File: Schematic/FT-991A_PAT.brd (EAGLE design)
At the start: 44.6 x 59.8 mm, 50 parts, among them Q1 SN74AHC-OR, Q10 PE4259, Q2 PE4259, Q3 NCP553, Q4 PE4259, Q5 J310, Q6 MC78L09ABDR2GOSCT, Q7 2SC5086, Q8 PE4259, Q9 PE4259, X1 IF_IN, X2 SCP_OUT, X3 SDR_OUT

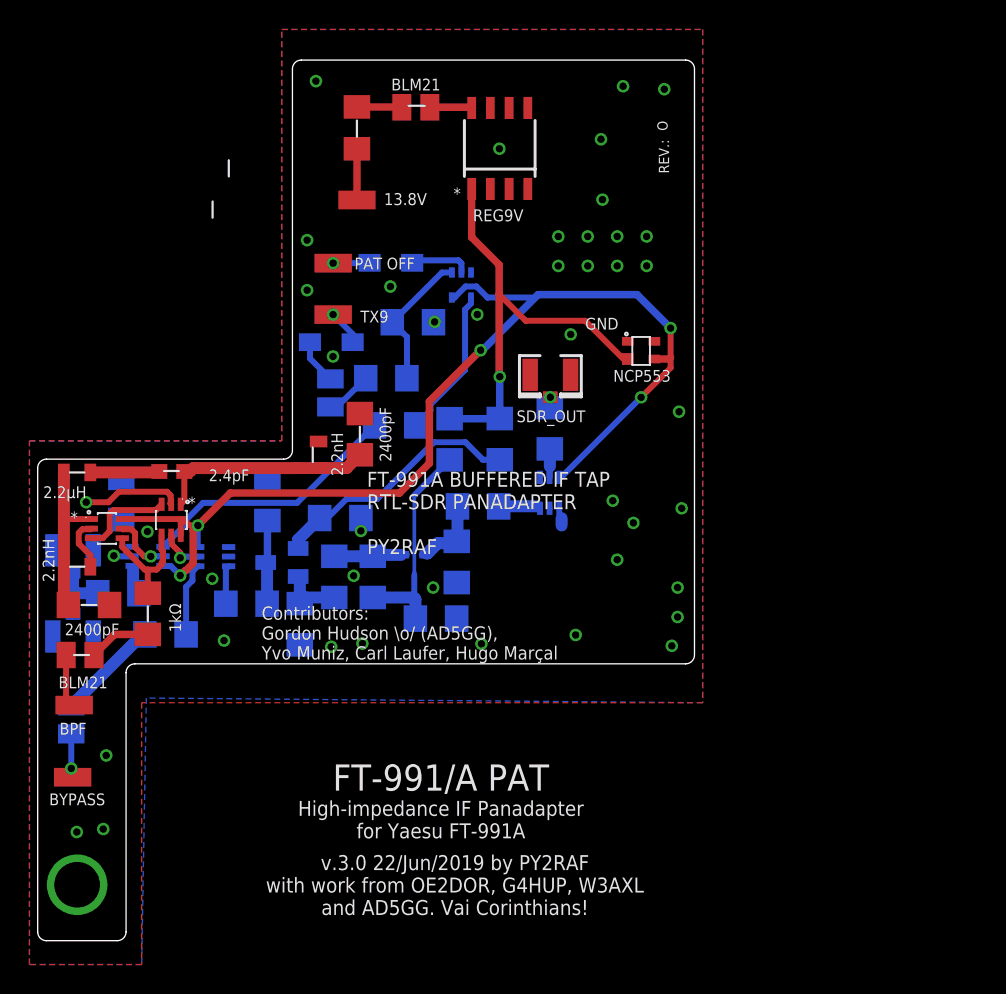
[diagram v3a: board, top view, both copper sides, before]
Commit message: Revision O: Moving toward golden
Components placed, new BPF design (tips hat to Karl-Anne SM0AOM)
Major board reorganization
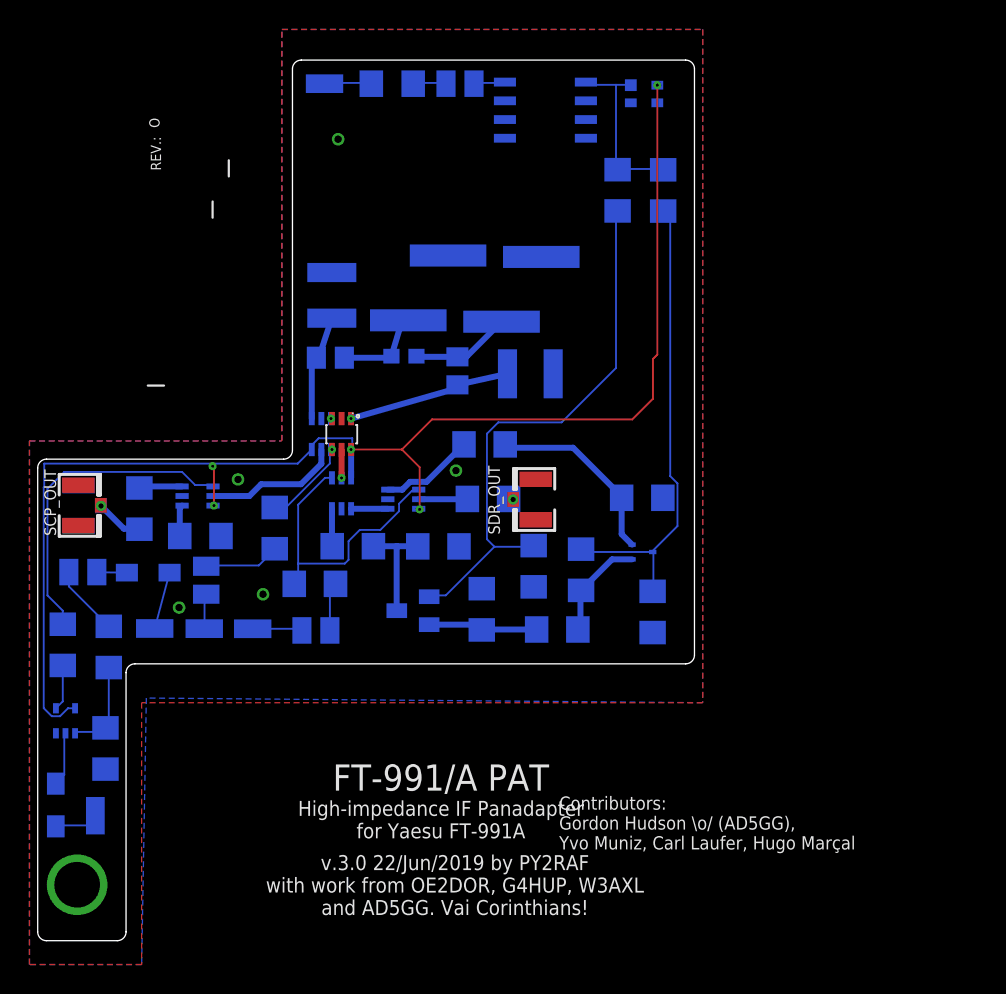
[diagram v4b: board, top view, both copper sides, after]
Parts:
- removed C3, C9: 2400pF, rcl:C3216
- removed C7: 2.4pF, rcl:C0603
- removed L4, L6: 2.2nH, aarf:0805
- removed L5: 2.2µH, aarf:0805
- removed PAD1: BPF, wirepad:SMD1,27-2,54
- removed PAD6: BYP, wirepad:SMD1,27-2,54
- added BPF: BPF, wirepad:SMD1,27-2,54
- added BYP: BYP, wirepad:SMD1,27-2,54
- added C10, C14: 62pF, rcl:C0805
- added C15, C16: 270pF, aarf:SQCB
- added C5: 1.5pF, rcl:C0603
- added L8, L9: 100nH, aarf:AIAC-1812
- PAD2: value PAT OFF -> DIS
- moved D1 43.3 mm to (7.55, 20.8), turned to 270 degrees
- moved PAD2 40.8 mm to (10.2, 20.1), flipped to the bottom, turned to 0 degrees
- moved Q1 40.0 mm to (8.21, 26.5), turned to 0 degrees
- moved R3 35.7 mm to (10.9, 24.7), turned to 270 degrees
- moved R6 27.1 mm to (8.03, 31.7), turned to 90 degrees
- moved R1 26.2 mm to (11.1, 31.6), turned to 90 degrees
- moved PAD3 24.5 mm to (14.3, 32.8), flipped to the bottom
- moved R10 22.3 mm to (48.8, 62.5)
- moved L2 20.8 mm to (9.39, 36.6), turned to 0 degrees
- moved D2 20.0 mm to (13.8, 36.6)
- moved R7 18.7 mm to (45.7, 62.6)
- moved L7 17.7 mm to (25.2, 32.7), turned to 0 degrees
- moved Q3 17.4 mm to (47.5, 69.1), flipped to the bottom, turned to 90 degrees
- moved Q2 15.9 mm to (25.6, 46.0), flipped to the bottom, turned to 180 degrees
- moved C8 15.6 mm to (41.6, 32.7), turned to 180 degrees
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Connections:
- removed net N$42: C7.2, L5.P$2
- removed net N$43: C7.1, C9.1, L6.P$2, Q9.1
- removed net N$7: C3.2, L4.P$2, L5.P$1, Q2.1
- new net N$12: C10.1, C5.1, L8.P$1
- new net N$30: C14.1, C5.2, L9.P$1
- new net N$31: C14.2, C16.P$1, Q9.1
- new net N$34: C10.2, C15.P$1, Q2.1
- net GNDA: now also C15.P$2, C16.P$2, L8.P$2, L9.P$2; no longer C3.1, C9.2, L4.P$1, L6.P$1
- net N$41: now also BYP.1; no longer PAD6.1
- net N$44: now also BPF.1; no longer PAD1.1
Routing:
- net N$9: track 17.5 -> 37.7 mm
- net VDD: track 76.2 -> 94.8 mm
- net VCC: track 30.1 -> 12.1 mm, vias 1 -> 0
- net N$10: track 14.6 -> 32.0 mm
- net N$40: track 4.96 -> 19.8 mm
- net N$43: track 14.7 -> 0.00 mm
- net GNDA: track 11.6 -> 0.00 mm, vias 45 -> 6
- net N$31: track 0.00 -> 11.3 mm, vias 0 -> 1
- net N$7: track 11.0 -> 0.00 mm
- net N$1: track 5.15 -> 12.9 mm
- net N$34: track 0.00 -> 7.26 mm
- net N$30: track 0.00 -> 7.06 mm
- net N$22: track 10.2 -> 3.18 mm
- net N$48: track 6.42 -> 0.07 mm, vias 0 -> 1
- net N$12: track 0.00 -> 6.30 mm
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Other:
- board text removed: "*"
- board text removed: "13.8V"
- board text removed: "5086"
- board text removed: "AND"
- board text removed: "BPF"
- board text removed: "BYPASS"
- board text removed: "FT-991A BUFFERED IF TAP RTL-SDR PANADAPTER PY2RAF"
- board text removed: "GND"
- board text removed: "PY2RAF"
- board text removed: "REG9V"
- board text removed: "VAI CORINTHIANS!"

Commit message: More Rev. O Advancements
Reviewed Ground Plane
Added (lots of) ground plane vias
Renumbered parts
Ran DRC and fixed a lot of airwires
A few component positioning hacks
Updated the Project Overview Block Diagram sheet
Updated credits
Removed obsolete amplifier LTSPICE file
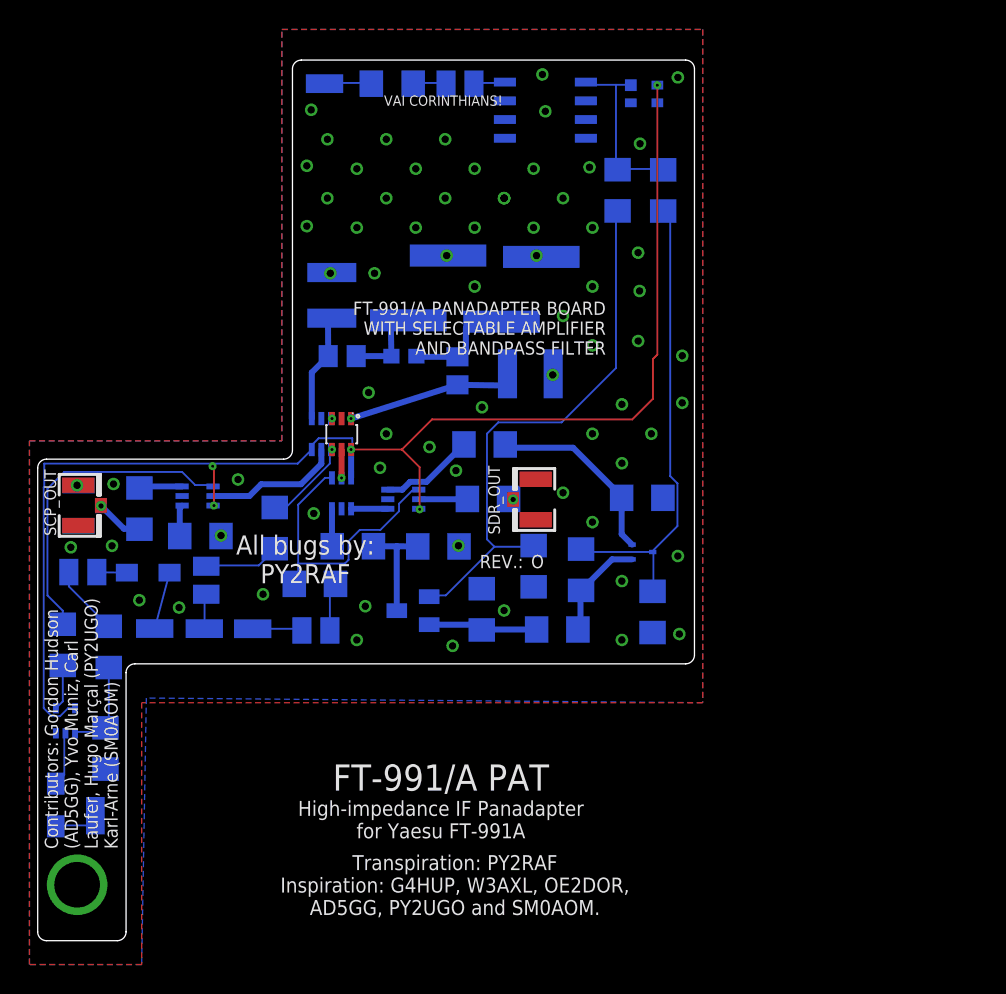
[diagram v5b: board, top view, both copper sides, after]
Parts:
- removed BPF: BPF, wirepad:SMD1,27-2,54
- removed C14: 62pF, rcl:C0805
- removed C15: 270pF, aarf:SQCB
- removed R12: 1kΩ, rcl:R3216
- added C3: 62pF, rcl:C0805
- added C7: 0.1µF, rcl:C3216
- added PAD1: 13.8V, wirepad:SMD1,27-2,54
- added R4: 5.6kΩ, rcl:R3216
- C10: value 62pF -> 1nF; device rcl:C0805 -> rcl:C3216
- C4: value 1nF -> 270pF; device rcl:C3216 -> aarf:SQCB
- C6: value 0.1µF -> 1nF
- C8: value 1nF -> 62pF; device rcl:C3216 -> rcl:C0805
- PAD2: value DIS -> BPF
- PAD4: value 13.8V -> DIS
- Q1: value SN74AHC-OR -> PE4259; device aarf:SC70-5 -> aarf:SC-70
- Q2: value PE4259 -> MC78L09ABDR2GOSCT; device aarf:SC-70 -> aarf:SOIC8
- Q3: value NCP553 -> SN74AHC-OR; device aarf:SC-82AB -> aarf:SC70-5
- Q5: value J310 -> NCP553; device transistor-fet:SOT23 -> aarf:SC-82AB
- Q6: value MC78L09ABDR2GOSCT -> PE4259; device aarf:SOIC8 -> aarf:SC-70
- Q7: value 2SC5086 -> J310; device aarf:2-2H1A -> transistor-fet:SOT23
- Q8: value PE4259 -> 2SC5086; device aarf:SC-70 -> aarf:2-2H1A
- R1: value 10kΩ -> 1kΩ
- R10: value 1kΩ -> 100Ω
- R11: value 100Ω -> 1kΩ
- R3: value 5.6kΩ -> 10kΩ
- R6: value 1kΩ -> 220Ω
- R7: value 220Ω -> 1kΩ
- R8: value 1kΩ -> 39kΩ
- R9: value 39kΩ -> 1kΩ
- moved Q3 57.9 mm to (8.21, 26.5), turned to 0 degrees
- moved PAD4 52.1 mm to (10.2, 20.1), turned to 0 degrees
- moved R6 48.7 mm to (45.7, 62.6)
- moved L2 41.9 mm to (35.0, 69.8)
- moved L3 41.9 mm to (9.39, 36.6)
- moved Q5 38.4 mm to (47.5, 69.1), turned to 90 degrees
- moved R7 29.9 mm to (36.5, 34.1), turned to 270 degrees
- moved Q6 29.5 mm to (27.0, 42.0), turned to 0 degrees
- moved Q2 26.7 mm to (40.8, 68.0), turned to 270 degrees
- moved R9 26.4 mm to (48.8, 62.5)
- moved C10 24.0 mm to (41.6, 32.7), turned to 180 degrees
- moved R11 23.0 mm to (25.1, 35.8)
- moved R10 20.9 mm to (47.4, 41.7), turned to 180 degrees
- moved Q8 20.8 mm to (47.4, 38.0), turned to 90 degrees
- moved C8 18.8 mm to (34.8, 50.3), turned to 270 degrees
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- renumbered BYP to PAD5, C16 to C9, L7 to L6, L8 to L4, L9 to L5
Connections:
- net GNDA: now also C4.P$2, C7.2, Q1.2, Q2.3, Q2.6, Q2.7, Q3.3, Q5.1, R10.2, R4.2, R7.1; no longer C15.P$2, C6.2, Q1.3, Q3.1, Q6.3, Q6.6, Q6.7, Q8.2, R11.2, R3.2, R8.1
- net N$1: now also Q8.2, R10.1; no longer Q7.2, R11.1
- net N$10: now also Q8.3, R8.1, R9.2; no longer Q7.3, R10.2, R9.1
- net N$12: now also C3.1; no longer C10.1
- net N$16: now also D2.A, PAD4.1; no longer D1.A, PAD2.1
- net N$18: now also D1.A; no longer D2.A
- net N$19: now also Q1.4, R2.2; no longer Q4.4, R6.2
- net N$20: now also D2.C, Q3.2; no longer D1.C, Q1.2
- net N$21: now also Q1.1; no longer Q4.1
- net N$22: now also Q3.4, R2.1; no longer Q1.4, R6.1
- net N$23: now also R11.2; no longer R12.2
- net N$24: now also Q1.3; no longer Q4.3
- net N$25: now also L3.2, R3.2; no longer L2.2, R1.2
- net N$26: now also L2.1, Q2.8; no longer L3.1, Q6.8
- net N$28: now also PAD1.1; no longer PAD4.1
- net N$29: now also C6.1, Q6.3; no longer C4.1, Q8.3
- net N$30: now also C8.1; no longer C14.1
- net N$31: now also C8.2; no longer C14.2
- net N$32: now also L2.2; no longer L3.2
- net N$33: now also Q6.1; no longer Q8.1
- net N$34: now also C3.2, C4.P$1, Q4.1; no longer C10.2, C15.P$1, Q2.1
- net N$35: now also D1.C, L3.1; no longer D2.C, L2.1
- net N$4: now also C10.2, Q8.1, R8.2; no longer C8.2, Q7.1, R9.2
- net N$40: now also Q6.4, R11.1; no longer Q8.4, R12.1
- net N$44: now also PAD2.1; no longer BPF.1
- net N$45: now also R1.2; no longer R2.2
- net N$46: now also Q4.4, R1.1; no longer Q2.4, R2.1
- net N$47: now also Q1.5; no longer Q2.5
- net N$48: now also Q4.3; no longer Q2.3
- net N$49: now also Q6.5; no longer Q8.5
- net N$5: now also C10.1, Q7.2, R7.2; no longer C8.1, Q5.2, R8.2
- net N$6: now also C6.2, Q7.3; no longer C4.2, Q5.3
- net N$8: now also Q3.1, R4.1; no longer Q1.1, R1.1
- net N$9: now also C7.1, Q7.1, R6.1; no longer C6.1, Q5.1, R7.1
- net VCC: now also Q2.1, Q5.2, R6.2, R9.1; no longer Q3.2, Q6.1, R10.1, R7.2
- net VDD: now also Q1.6, Q3.5, Q5.3, Q6.6; no longer Q1.5, Q2.6, Q3.3, Q8.6
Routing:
- net N$6: track 10.5 -> 7.38 mm
- net N$33: track 4.93 -> 2.49 mm
- net N$8: track 7.35 -> 6.47 mm
- net N$30: track 7.06 -> 7.60 mm
- net N$47: track 9.75 -> 9.23 mm
- net N$31: track 11.3 -> 11.9 mm
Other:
- board text added: "All bugs by: PY2RAF"
- board text added: "Contributors: Gordon Hudson (AD5GG), Yvo Muniz, Carl Laufer, Hugo Marçal (PY2UGO) Karl-Arne (SM0AOM)"
- board text added: "FT-991/A PANADAPTER BOARD WITH SELECTABLE AMPLIFIER AND BANDPASS FILTER"
- board text added: "Transpiration: PY2RAF Inspiration: G4HUP, W3AXL, OE2DOR, AD5GG, PY2UGO and SM0AOM."
- board text added: "VAI CORINTHIANS!"
- board text removed: "Contributors: Gordon Hudson \\o/ (AD5GG), Yvo Muniz, Carl Laufer, Hugo Marçal"
- board text removed: "v.3.0 22/Jun/2019 by PY2RAF with work from OE2DOR, G4HUP, W3AXL and AD5GG. Vai Corinthians!"

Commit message: Revision O: A few minor (toward GA) changes
Minor board labelling enhancements
Updated BOM, Gerber and Readme
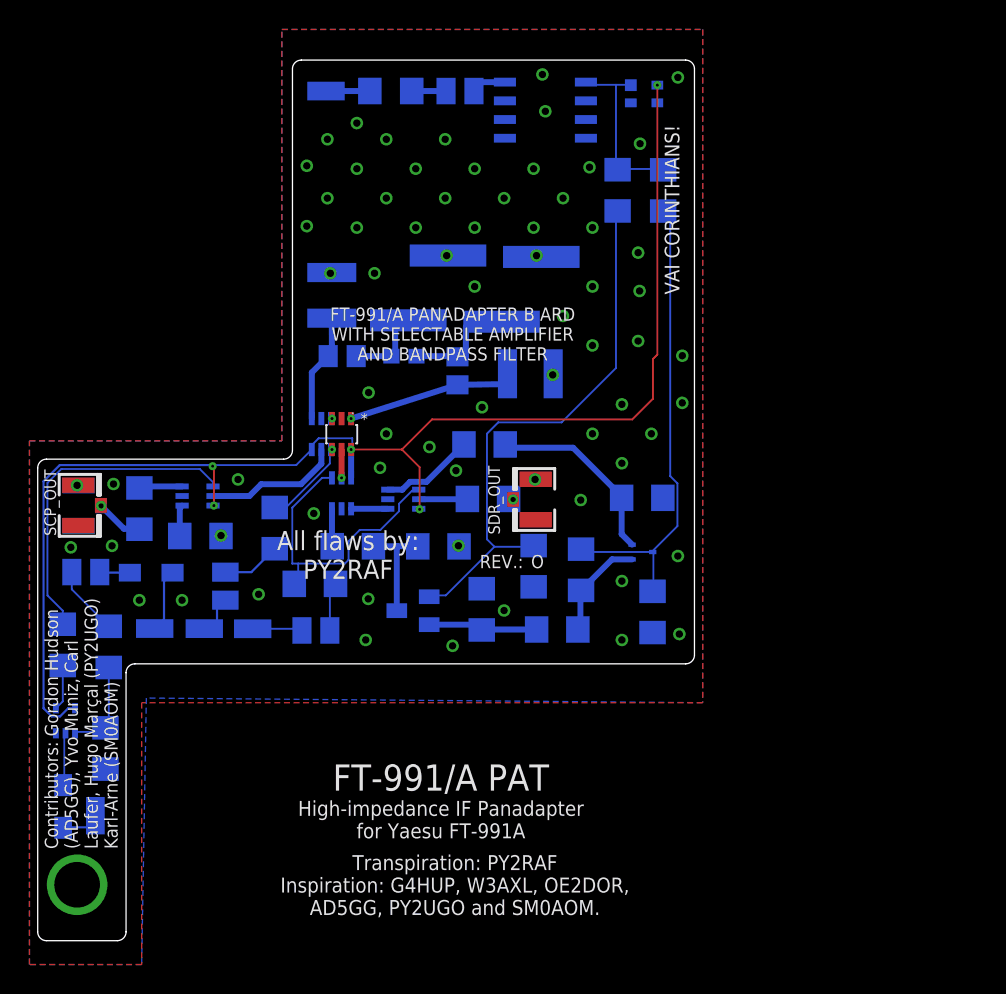
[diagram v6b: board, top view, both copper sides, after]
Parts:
- removed PAD1: 13.8V, wirepad:SMD1,27-2,54
- added 13.8V: 13.8V, wirepad:SMD1,27-2,54
- F1: value 150 mA -> 150mA
- Q8: value 2SC5086 -> 5086
- moved L1 1.36 mm to (19.1, 35.7)
- moved D2 0.51 mm to (8.05, 20.7)
- moved F1 0.51 mm to (30.3, 69.3)
- moved L2 0.50 mm to (35.0, 69.3)
- moved D1 0.20 mm to (14.0, 36.6)
- moved L3 0.20 mm to (9.59, 36.6)
- renumbered PAD2 to BPF, PAD5 to BYP
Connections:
- net N$28: now also 13.8V.1; no longer PAD1.1
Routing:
- net N$45: track 5.19 -> 4.01 mm
- net N$44: track 2.40 -> 3.17 mm
- net VDD: track 94.7 -> 94.0 mm
- net N$40: track 19.8 -> 20.5 mm
- net N$19: track 21.8 -> 22.3 mm
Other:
- board text added: "All flaws by: PY2RAF"
- board text added: "FT-991/A PANADAPTER B ARD WITH SELECTABLE AMPLIFIER AND BANDPASS FILTER"
- board text removed: "All bugs by: PY2RAF"
- board text removed: "FT-991/A PANADAPTER BOARD WITH SELECTABLE AMPLIFIER AND BANDPASS FILTER"

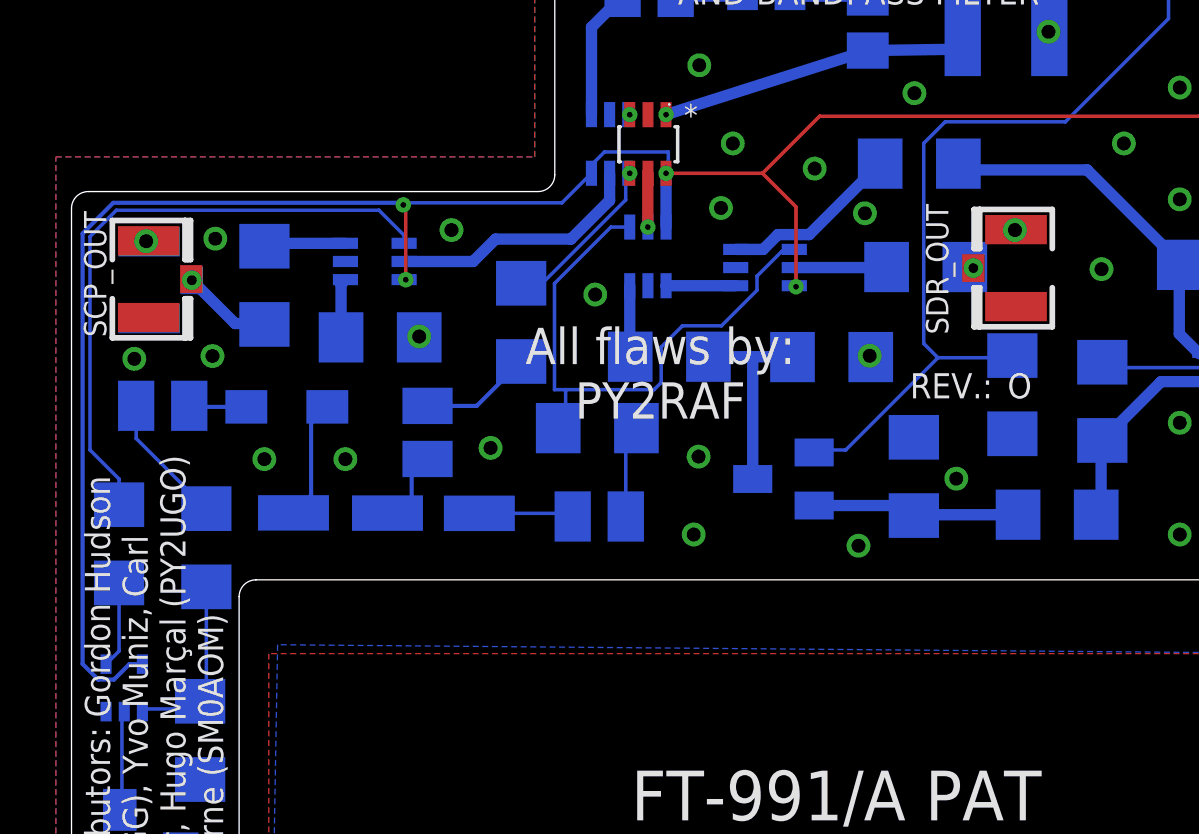
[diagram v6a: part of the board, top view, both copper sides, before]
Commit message: Starring: Revision P, Full Version
* Changed RF switch layout - now IF input uses the RF switch's `RFC`
  port instead of RF2 - It seems that the PE4259's `RF{N}` port gets in
  a grounded state instead of just reflecting out the data when the port
  is not selected/active
* Got rid of the "Grounding" in RF1 port; that's not necessary
  because... Above
* Because of that... One less component (the 4.7 nF C2 cap)
* Updated BOM to reflect capacitor removal - also reorganized it
* Few component routing/placement for better ground plane rastnest
* Updated Bandpass .ASC file for use with LTSpice; reflects SM0AOM
  filter, with new values
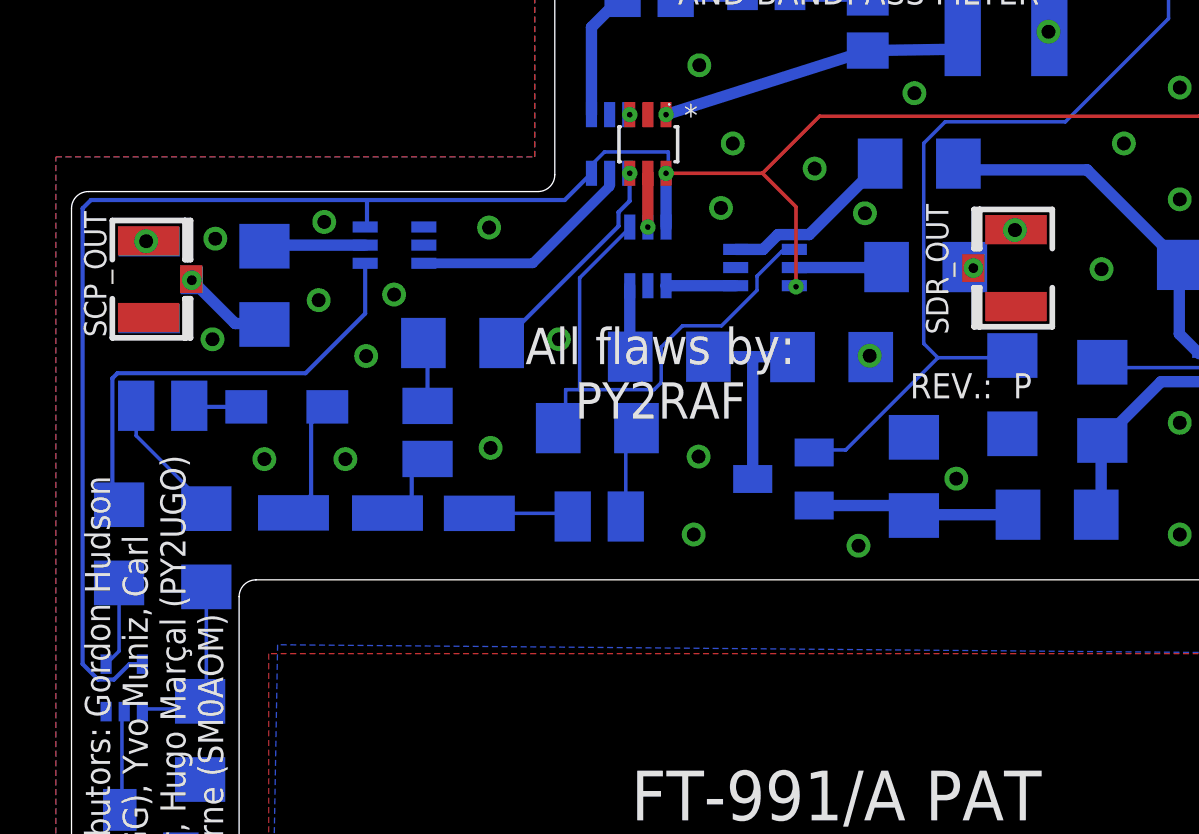
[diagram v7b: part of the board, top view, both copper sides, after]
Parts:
- removed C2: 4.7nF, rcl:C3216
- F1: value 150mA -> 50mA
- Q1: value PE4259 -> (none)
- moved R1 2.23 mm to (20.3, 38.9), turned to 0 degrees
- moved Q1 0.96 mm to (17.9, 42.4), turned to 270 degrees
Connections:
- removed net N$21: C2.2, Q1.1
- net GNDA: no longer C2.1
- net N$24: now also Q1.5; no longer Q1.3
- net N$47: now also Q1.3; no longer Q1.5
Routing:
- net N$19: track 22.3 -> 16.4 mm
- net N$21: track 2.13 -> 0.00 mm
- net N$46: track 6.02 -> 8.05 mm
- net N$45: track 4.01 -> 2.31 mm
- net VDD: track 94.0 -> 92.6 mm, vias 5 -> 3
- net N$40: track 20.5 -> 19.4 mm
- net N$47: track 9.23 -> 8.26 mm
- net N$24: track 2.94 -> 3.62 mm
